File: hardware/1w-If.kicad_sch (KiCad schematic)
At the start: 50 parts, among them U1 WT32-ETH01, U2 TCA9548APWR, U3 DS2484R, U4 DS2484R, U5 DS2484R, U6 DS2484R, X1 PowerSupply, X2 Debug Terminal, X3 Ext LED Terminal, X4 1-Wire Ch1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

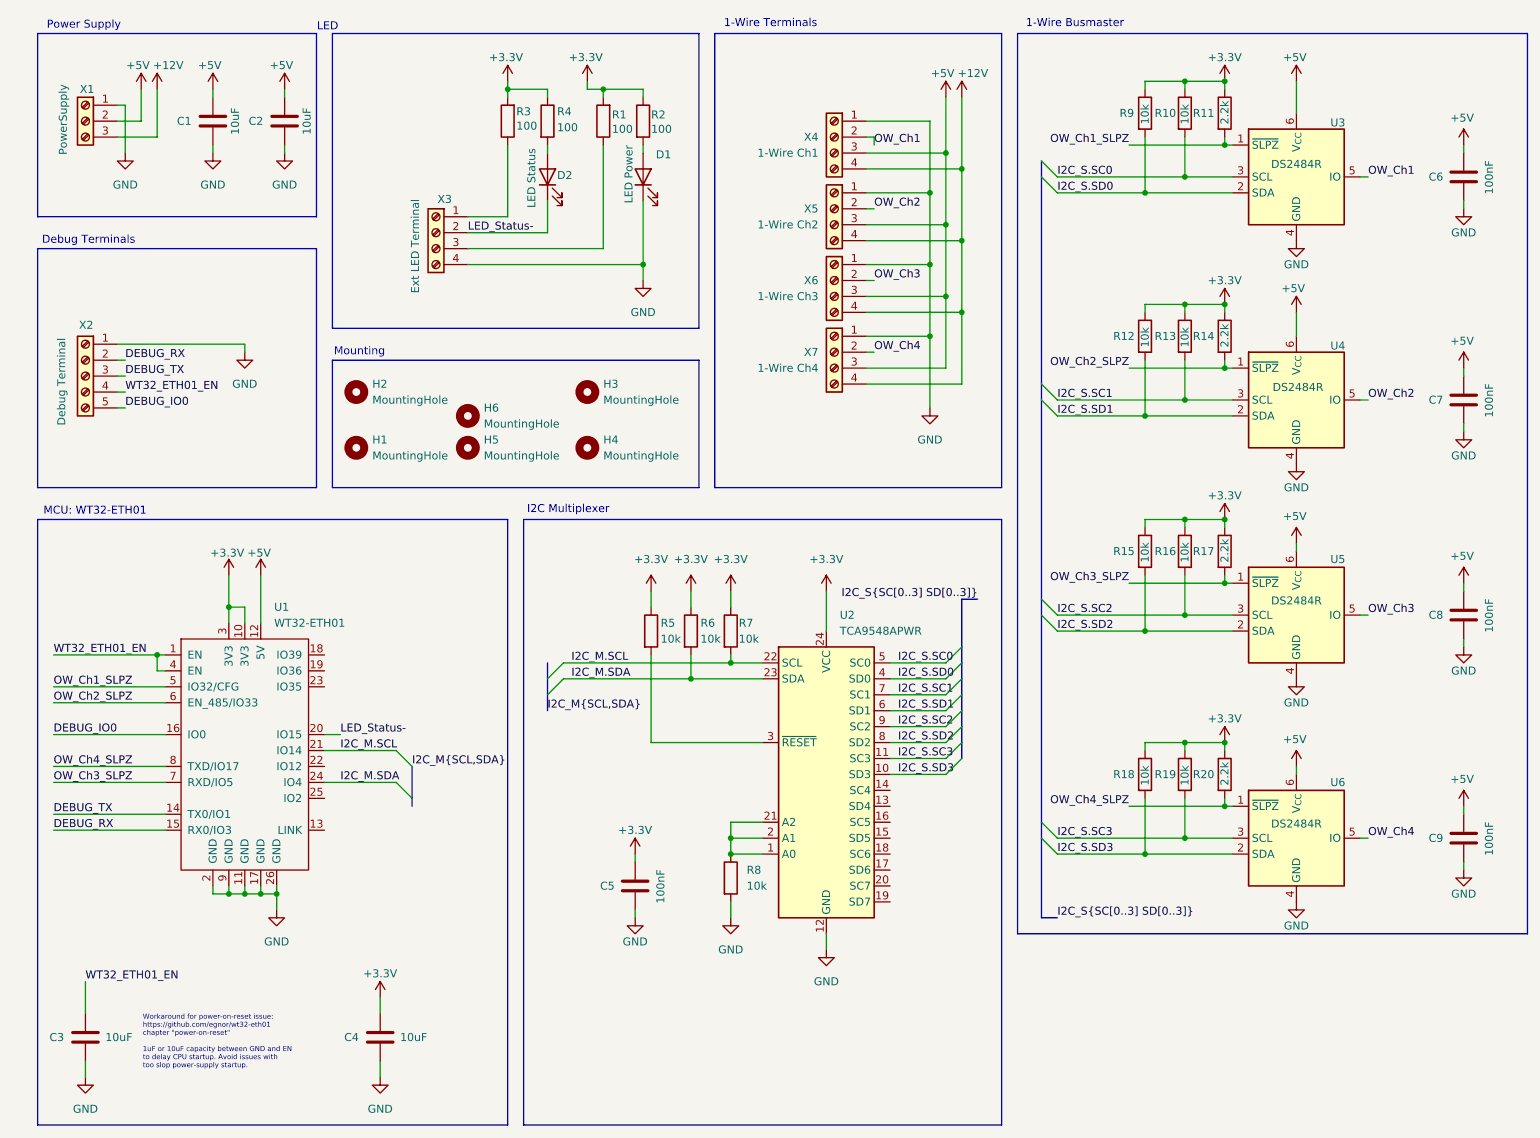
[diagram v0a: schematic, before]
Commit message: C1-C4: Fix polarity | R1+R3: Adapt for 20mA external LEDs
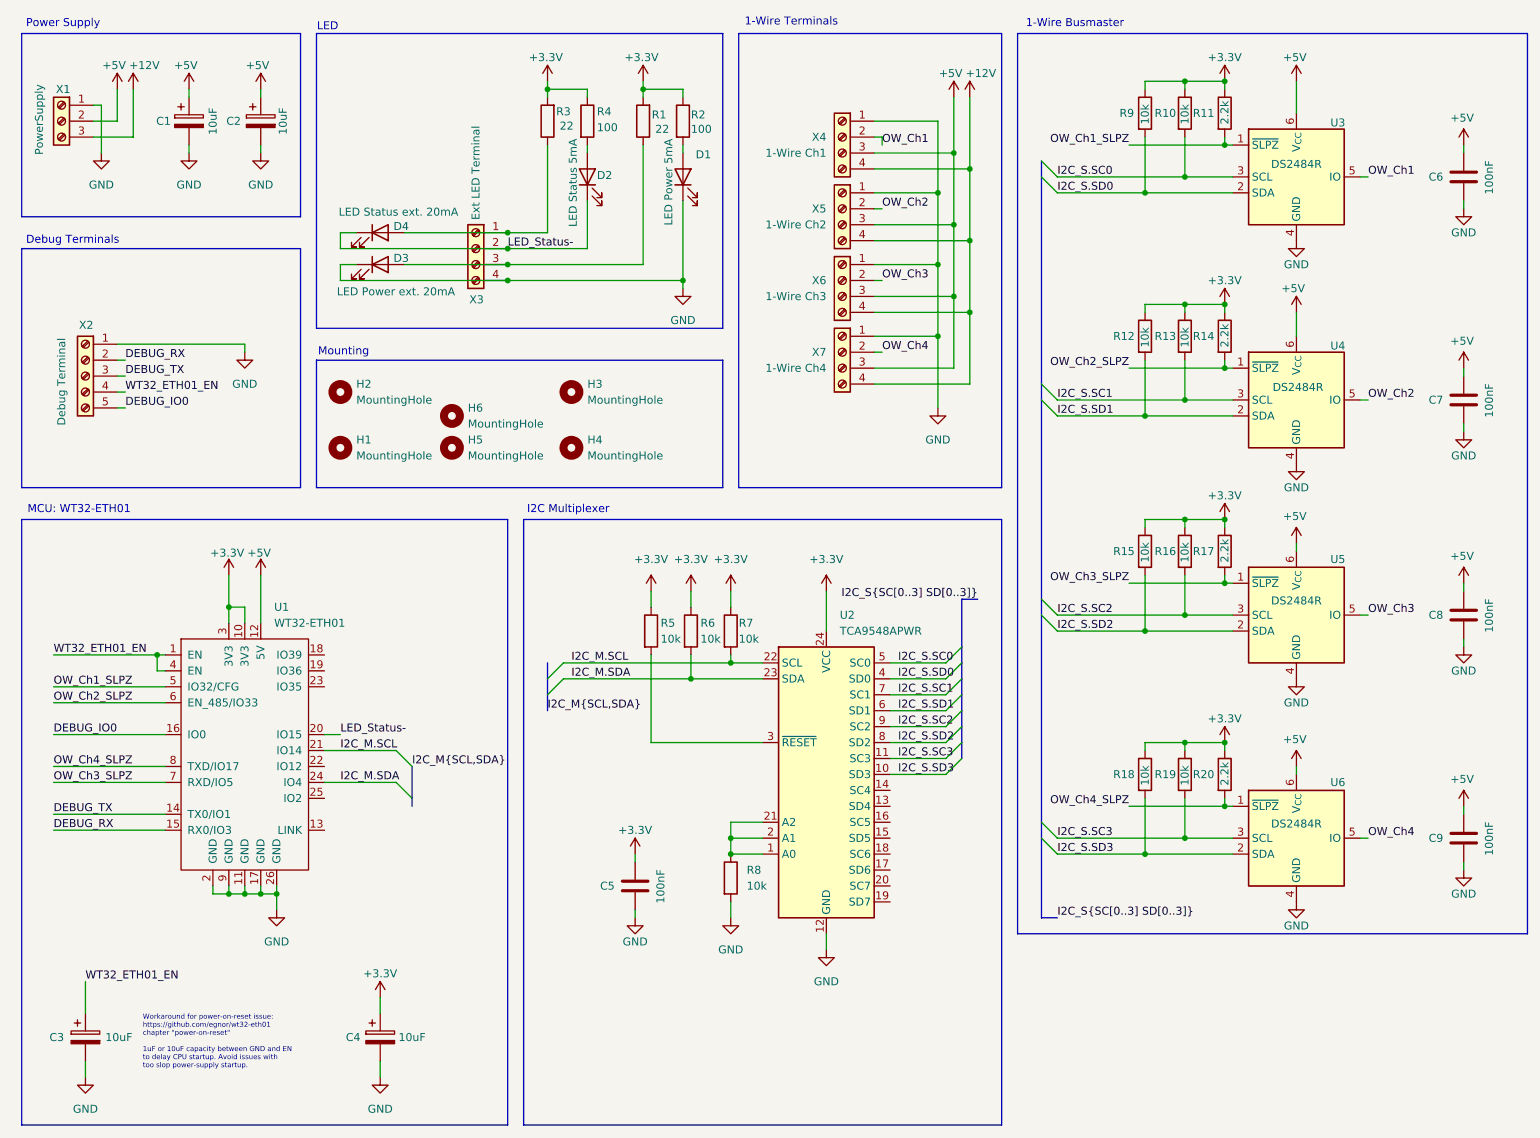
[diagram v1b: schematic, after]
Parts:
- added D3: LED Power ext. 20mA, LED_SMD:LED_0805_2012Metric_Pad1.15x1.40mm_HandSolder, symbol Device:LED
- added D4: LED Status ext. 20mA, LED_SMD:LED_0805_2012Metric_Pad1.15x1.40mm_HandSolder, symbol Device:LED
- C1, C2, C3, C4: symbol Device:C -> Device:C_Polarized
- D1: value LED Power -> LED Power 5mA
- D2: value LED Status -> LED Status 5mA
- R1, R3: value 100 -> 22
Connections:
- net +3.3V: now also C4.1; no longer C4.2
- net +5V: now also C1.1, C2.1; no longer C1.2, C2.2
- net GND: now also C1.2, C2.2, C3.2, C4.2, D3.1 (K); no longer C1.1, C2.1, C3.1, C4.1
- net LED_Status-: now also D4.1 (K)
- net WT32_ETH01_EN: now also C3.1; no longer C3.2
- net at R3.1, X3.1 (Pin_1): now also D4.2 (A)
- net at R1.1, X3.3 (Pin_3): now also D3.2 (A)
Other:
- moved on the sheet: D1, D2, H1, H2, H3, H4, H5, H6, R1, R2, R3, R4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

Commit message: - Too bright LEDs: R1-R4 changed to 1kOhm - Swapped ext. LED connector silk layer description
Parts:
- R1, R3: value 22 -> 1k
- R2, R4: value 100 -> 1k
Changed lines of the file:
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@@
 			)
 		)
-		(property "Value" "100"
+		(property "Value" "1k"
 			(at 125.73 36.83 0)
 			(effects
@@
 			)
 		)
-		(property "Value" "22"
+		(property "Value" "1k"
 			(at 121.158 36.83 0)
 			(effects
@@
 			)
 		)
-		(property "Value" "100"
+		(property "Value" "1k"
 			(at 110.744 36.576 0)
 			(effects
@@
 			)
 		)
-		(property "Value" "22"
+		(property "Value" "1k"
 			(at 105.918 36.322 0)
 			(effects

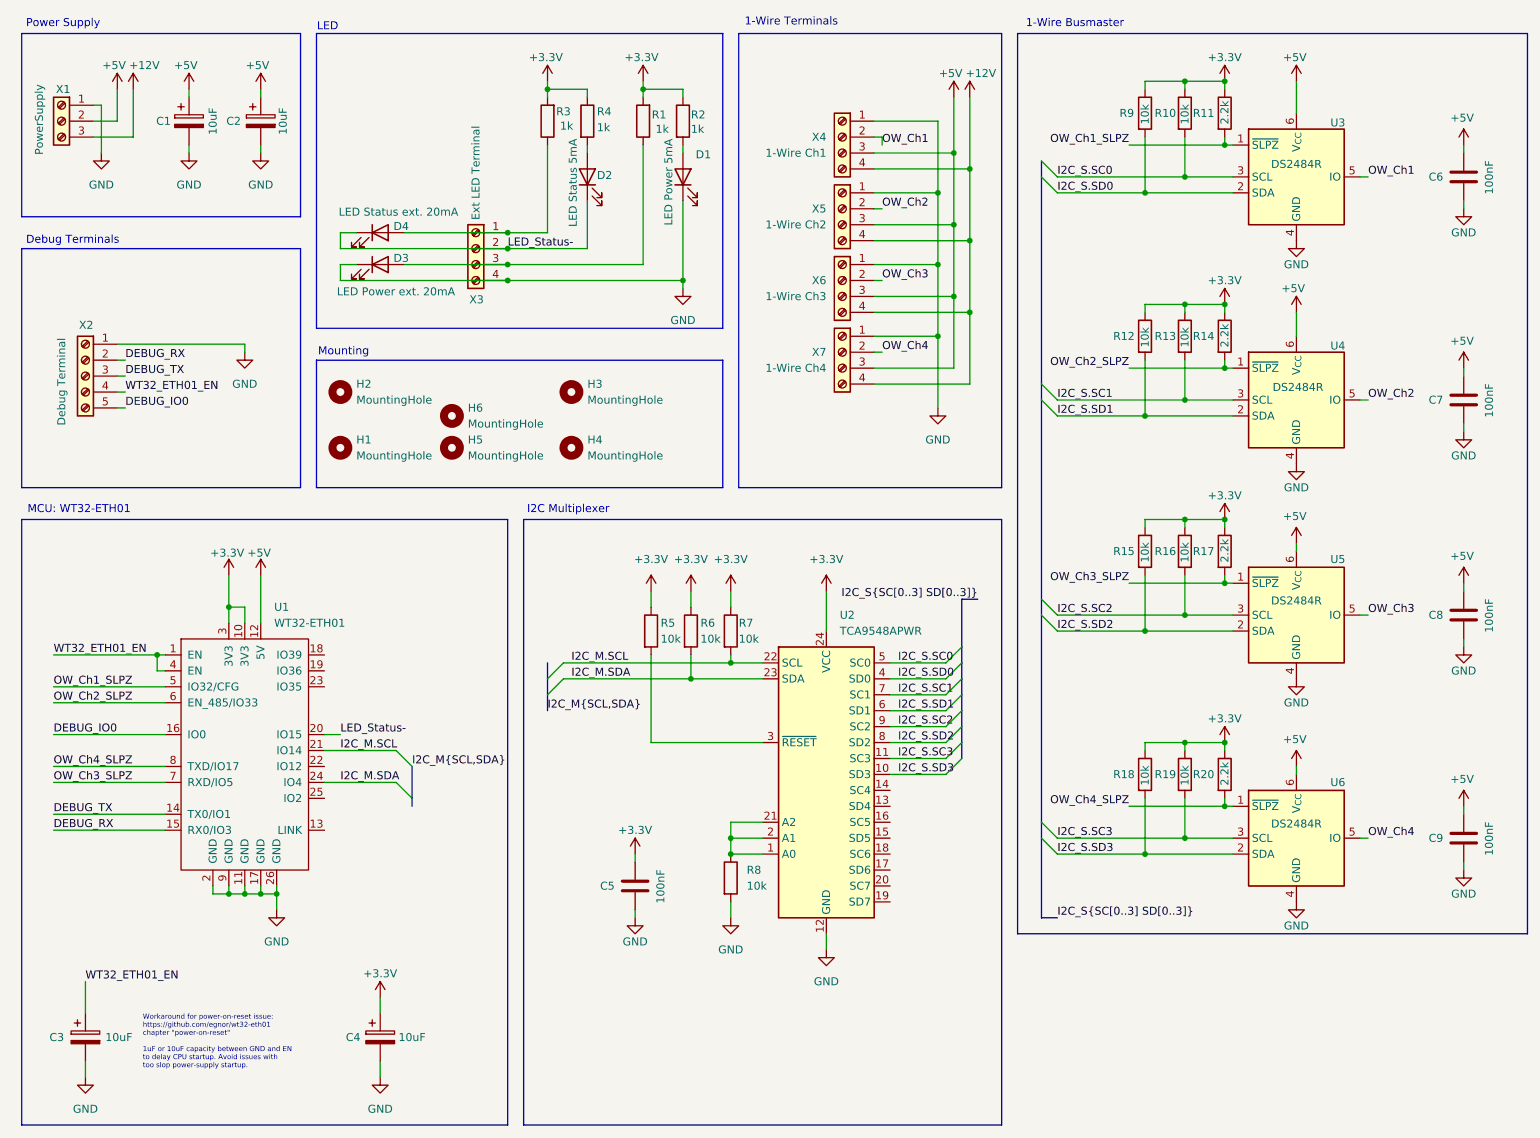
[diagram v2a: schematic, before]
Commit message: Added pin connectors for WT32_ETH01 Reworked BOM / datasheets
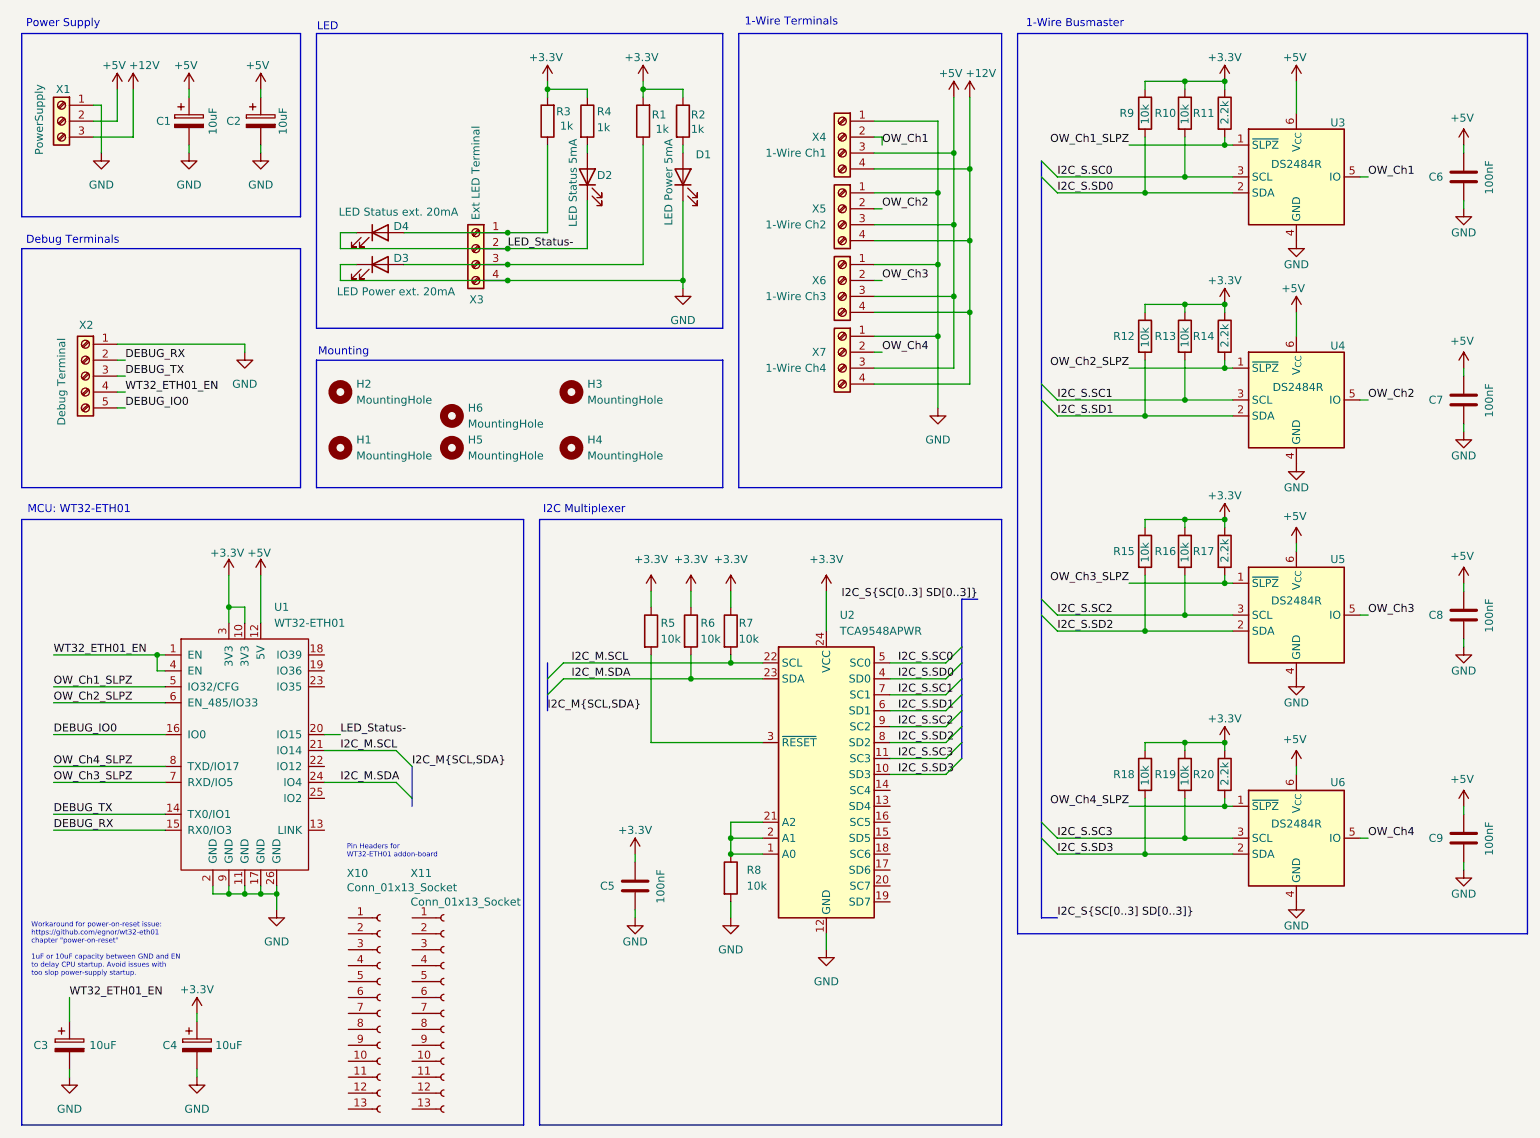
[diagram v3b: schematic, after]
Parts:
- added X10, X11: Conn_01x13_Socket, symbol Connector:Conn_01x13_Socket
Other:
- note added: "Pin Headers for WT32-ETH01 addon-board"
- moved on the sheet: C3, C4
